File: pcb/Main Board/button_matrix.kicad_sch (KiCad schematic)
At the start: 24 parts, among them SW1 SW_Push, SW2 SW_Push, SW3 SW_Push, SW4 SW_Push, SW5 SW_Push, SW6 SW_Push, SW7 SW_Push, SW8 SW_Push

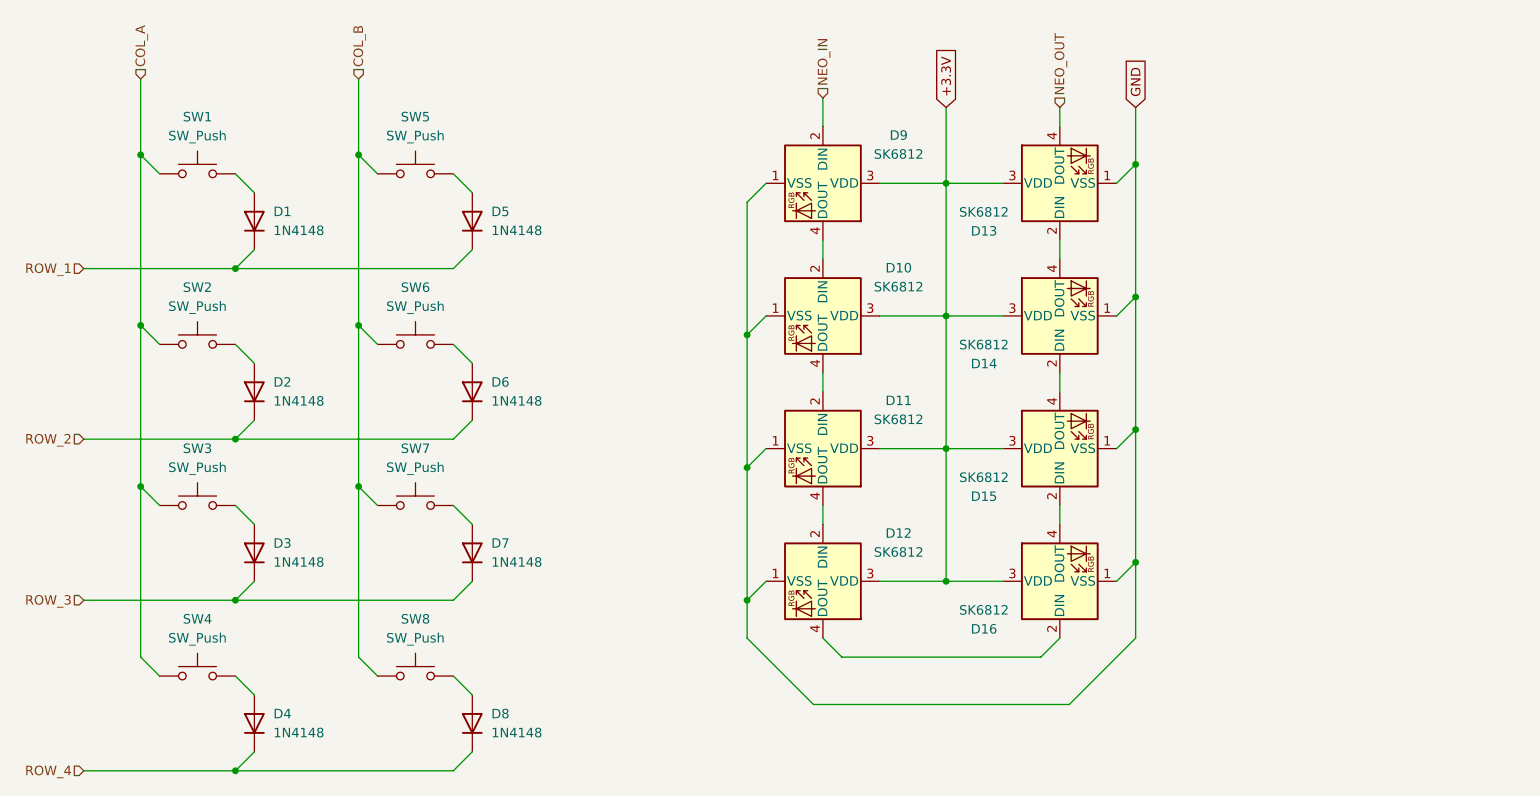
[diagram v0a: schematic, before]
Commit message: Create 4960 symbol and footprint
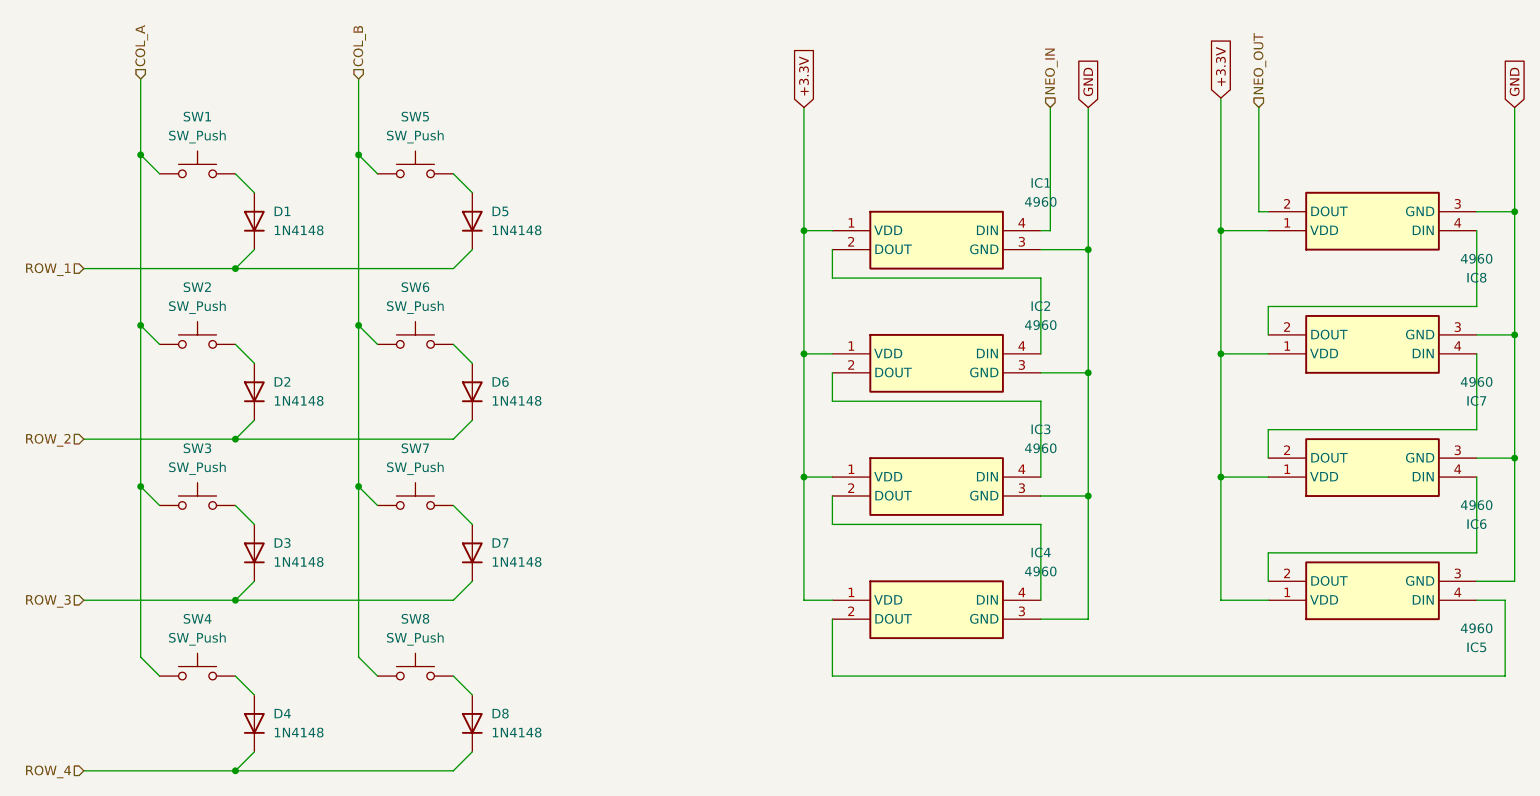
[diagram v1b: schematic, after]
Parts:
- removed D10, D11, D12, D13, D14, D15, D16, D9: SK6812, LED_SMD:LED_SK6812_PLCC4_5.0x5.0mm_P3.2mm, symbol LED:SK6812
- added IC1, IC2, IC3, IC4, IC5, IC6, IC7, IC8: 4960, Transmitter Library:4960_ADA, symbol Transmitter Symbol Library:4960
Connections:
- net +3.3V: now also IC1.1 (VDD), IC2.1 (VDD), IC3.1 (VDD), IC4.1 (VDD), IC5.1 (VDD), IC6.1 (VDD), IC7.1 (VDD), IC8.1 (VDD)
- net GND: now also IC1.3 (GND), IC2.3 (GND), IC3.3 (GND), IC4.3 (GND), IC5.3 (GND), IC6.3 (GND), IC7.3 (GND), IC8.3 (GND)
- net NEO_IN: now also IC1.4 (DIN)
- net NEO_OUT: now also IC8.2 (DOUT)
- new net: IC4.2 (DOUT), IC5.4 (DIN)
- new net: IC3.2 (DOUT), IC4.4 (DIN)
- new net: IC2.2 (DOUT), IC3.4 (DIN)
- new net: IC1.2 (DOUT), IC2.4 (DIN)
- new net: IC5.2 (DOUT), IC6.4 (DIN)
- new net: IC7.2 (DOUT), IC8.4 (DIN)
- new net: IC6.2 (DOUT), IC7.4 (DIN)

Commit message: more more more routing
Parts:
- renumbered IC8 to IC5, IC7 to IC6, IC6 to IC7, IC5 to IC8
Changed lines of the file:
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@@
 		(on_board yes)
 		(dnp no)
-		(property "Reference" "IC5"
+		(property "Reference" "IC8"
 			(at 231.14 115.57 0)
 			(effects
@@
 			(project "Transmitter Main Board"
 				(path "/ab8869b7-f9fd-4421-ad1e-15a14ea7e3d2/1af7f400-85d1-45c7-9de1-8b0a1cc91110"
-					(reference "IC5")
+					(reference "IC8")
 					(unit 1)
 				)
@@
 		(on_board yes)
 		(dnp no)
-		(property "Reference" "IC7"
+		(property "Reference" "IC6"
 			(at 231.14 82.55 0)
 			(effects
@@
 			(project "Transmitter Main Board"
 				(path "/ab8869b7-f9fd-4421-ad1e-15a14ea7e3d2/1af7f400-85d1-45c7-9de1-8b0a1cc91110"
-					(reference "IC7")
+					(reference "IC6")
 					(unit 1)
 				)
@@
 		(on_board yes)
 		(dnp no)
-		(property "Reference" "IC8"
+		(property "Reference" "IC5"
 			(at 231.14 66.04 0)
 			(effects
@@
 			(project "Transmitter Main Board"
 				(path "/ab8869b7-f9fd-4421-ad1e-15a14ea7e3d2/1af7f400-85d1-45c7-9de1-8b0a1cc91110"
-					(reference "IC8")
+					(reference "IC5")
 					(unit 1)
 				)
@@
 		(on_board yes)
 		(dnp no)
-		(property "Reference" "IC6"
+		(property "Reference" "IC7"
 			(at 231.14 99.06 0)
 			(effects
@@
 			(project "Transmitter Main Board"
 				(path "/ab8869b7-f9fd-4421-ad1e-15a14ea7e3d2/1af7f400-85d1-45c7-9de1-8b0a1cc91110"
-					(reference "IC6")
-					(unit 1)
-				)
+					(reference "IC7")
+					(unit 1)
+				)
